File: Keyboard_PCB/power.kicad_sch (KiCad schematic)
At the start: 9 parts, among them U5 ISL91127IRAZ

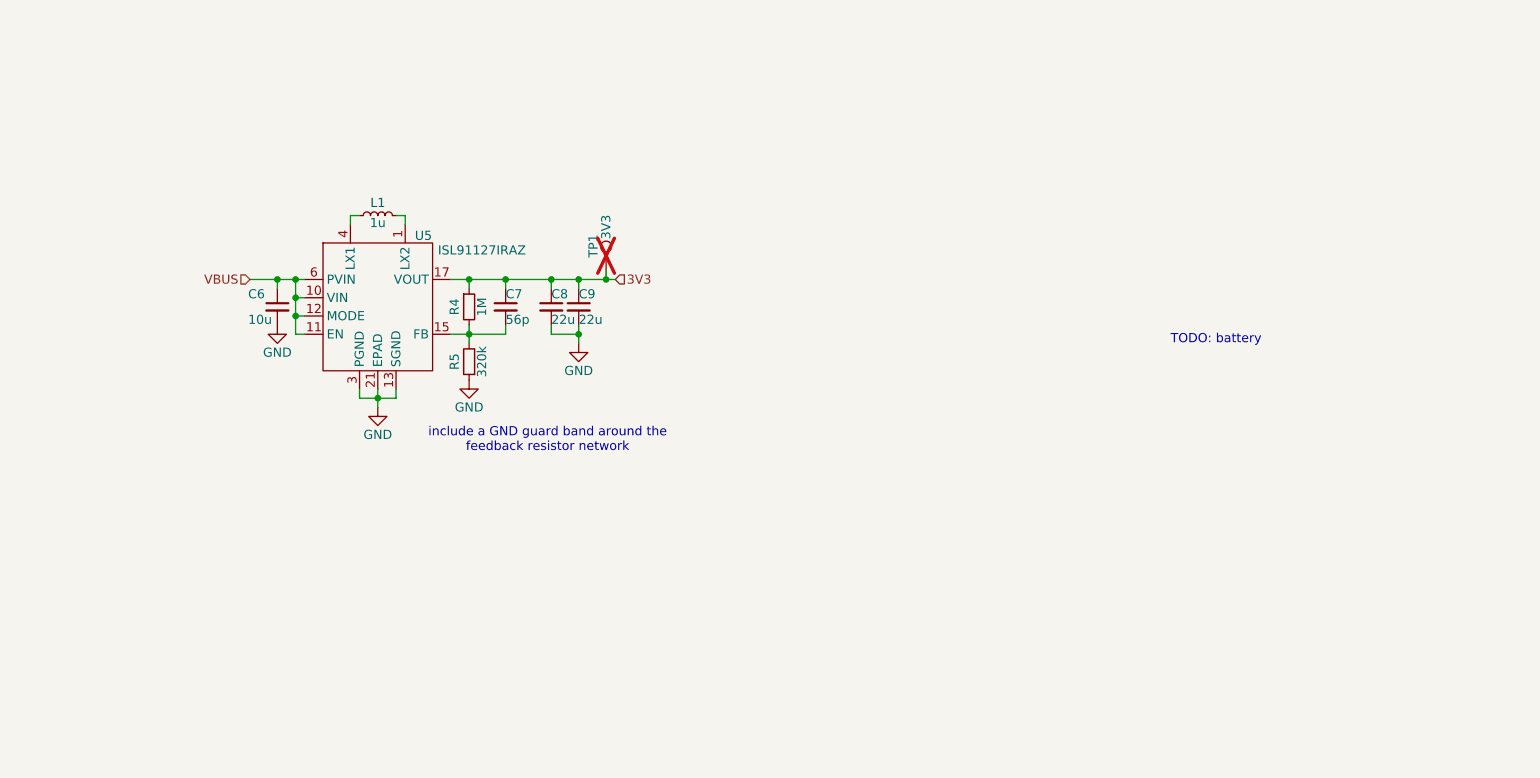
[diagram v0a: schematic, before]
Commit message: Schematic done
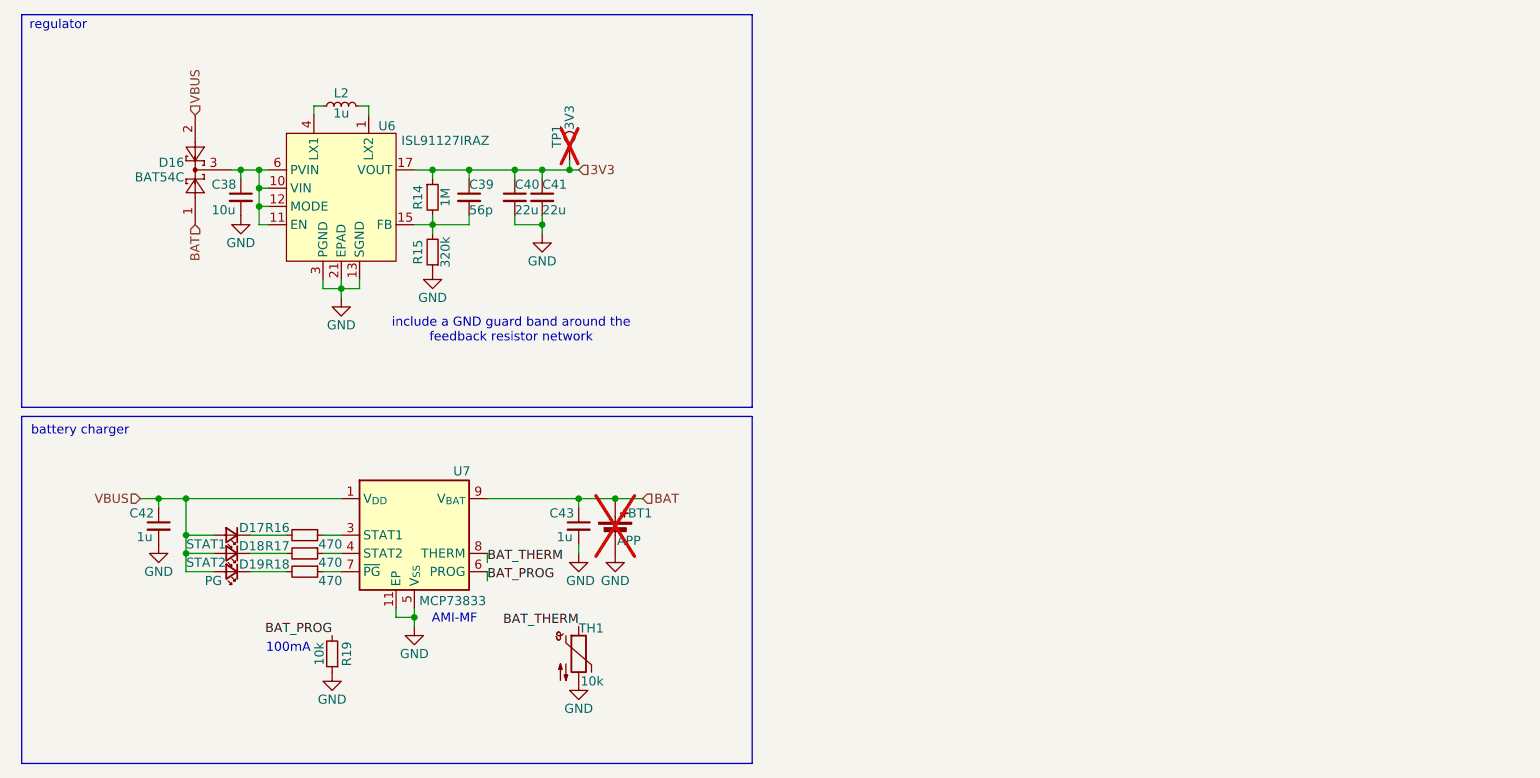
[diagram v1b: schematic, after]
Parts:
- added BT1: APP, Connector_PinHeader_2.54mm:PinHeader_1x02_P2.54mm_Vertical, symbol Device:Battery_Cell
- added C42, C43: 1u, Capacitor_SMD:C_0603_1608Metric, symbol Device:C_Small
- added D16: BAT54C, Package_TO_SOT_SMD:SOT-23, symbol Diode:BAT54C
- added D17: STAT1, LED_SMD:LED_0603_1608Metric, symbol Device:LED_Small
- added D18: STAT2, LED_SMD:LED_0603_1608Metric, symbol Device:LED_Small
- added D19: PG, LED_SMD:LED_0603_1608Metric, symbol Device:LED_Small
- added R16, R17, R18: 470, Resistor_SMD:R_0603_1608Metric, symbol Device:R_Small
- added R19: 10k, Resistor_SMD:R_0603_1608Metric, symbol Device:R_Small
- added TH1: 10k, Resistor_SMD:R_0603_1608Metric, symbol Device:Thermistor_NTC
- added U7: MCP73833, Package_DFN_QFN:DFN-10-1EP_3x3mm_P0.5mm_EP1.58x2.35mm, symbol Battery_Management:MCP73833-xxx-MF
- renumbered C6 to C38, C7 to C39, C8 to C40, C9 to C41, L1 to L2, R4 to R14, R5 to R15, U5 to U6
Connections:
- net GND: now also BT1.2 (-), C42.2, C43.2, R19.1, TH1.2, U7.11 (EP), U7.5 (V_{SS})
- net VBUS: now also C42.1, D16.2, D17.2 (A), D18.2 (A), D19.2 (A), U7.1 (V_{DD}), U7.2 (V_{DD}); no longer C38.1, U6.10 (VIN), U6.11 (EN), U6.12 (MODE), U6.6 (PVIN), U6.7 (PVIN), U6.8 (PVIN), U6.9 (PVIN)
- new net: C38.1, D16.3, U6.10 (VIN), U6.11 (EN), U6.12 (MODE), U6.6 (PVIN), U6.7 (PVIN), U6.8 (PVIN), U6.9 (PVIN)
- new net: R16.1, U7.3 (STAT1)
- new net: R17.1, U7.4 (STAT2)
- new net: R18.1, U7.7 (~{PG})
- new net: D18.1 (K), R17.2
- new net: D17.1 (K), R16.2
- new net: D19.1 (K), R18.2
- new net BAT: BT1.1 (+), C43.1, D16.1, U7.10 (V_{BAT}), U7.9 (V_{BAT})
- new net BAT_PROG: R19.2, U7.6 (PROG)
- new net BAT_THERM: TH1.1, U7.8 (THERM)
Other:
- note added: "100mA"
- note added: "AMI-MF"
- note added: "battery charger"
- note added: "regulator"
- note removed: "TODO: battery"
- moved on the sheet: C38, C39, C40, C41, L2, R14, R15, TP1

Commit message: eMMC routing and STM passives
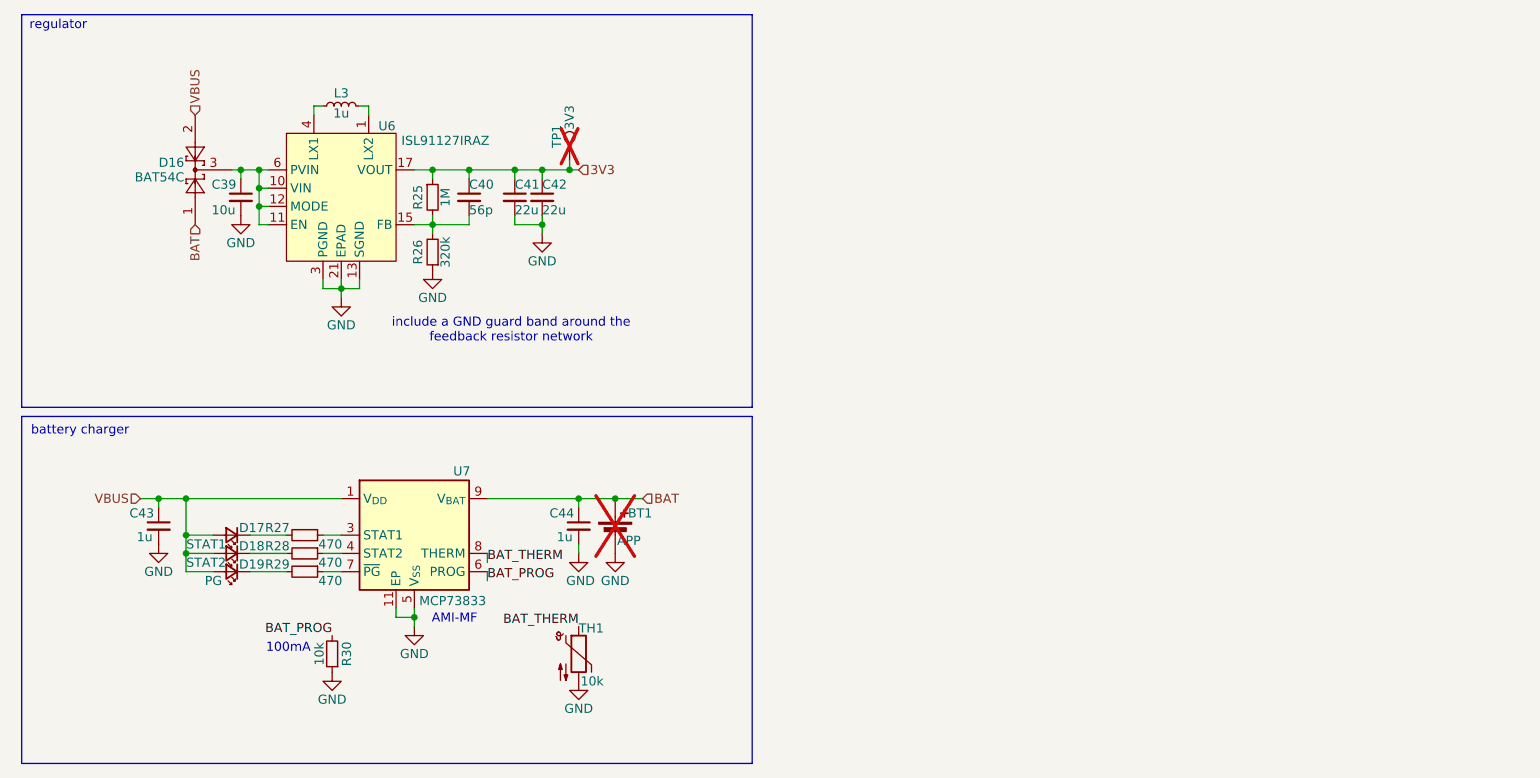
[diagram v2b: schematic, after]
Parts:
- renumbered C38 to C39, C39 to C40, C40 to C41, C41 to C42, C42 to C43, C43 to C44, L2 to L3, R14 to R25, R15 to R26, R16 to R27, R17 to R28, R18 to R29, R19 to R30
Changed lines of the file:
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@@
 		(on_board yes)
 		(dnp no)
-		(property "Reference" "C39"
+		(property "Reference" "C40"
 			(at 74.93 36.322 0)
 			(effects
@@
 			(project "Keyboard_PCB"
 				(path "/dd51e792-c76c-4d43-96de-494177f3b593/700844a0-d855-4a8d-a339-68e2adaa6562"
-					(reference "C39")
+					(reference "C40")
 					(unit 1)
 				)
@@
 		(on_board yes)
 		(dnp no)
-		(property "Reference" "#PWR068"
+		(property "Reference" "#PWR081"
 			(at 67.31 104.14 0)
 			(effects
@@
 			(project "Keyboard_PCB"
 				(path "/dd51e792-c76c-4d43-96de-494177f3b593/700844a0-d855-4a8d-a339-68e2adaa6562"
-					(reference "#PWR068")
+					(reference "#PWR081")
 					(unit 1)
 				)
@@
 		(on_board yes)
 		(dnp no)
-		(property "Reference" "C38"
+		(property "Reference" "C39"
 			(at 39.116 36.322 0)
 			(effects
@@
 			(project "Keyboard_PCB"
 				(path "/dd51e792-c76c-4d43-96de-494177f3b593/700844a0-d855-4a8d-a339-68e2adaa6562"
-					(reference "C38")
+					(reference "C39")
 					(unit 1)
 				)
@@
 		(on_board yes)
 		(dnp no)
-		(property "Reference" "R14"
+		(property "Reference" "R25"
 			(at 67.818 38.1 90)
 			(effects
@@
 			(project "Keyboard_PCB"
 				(path "/dd51e792-c76c-4d43-96de-494177f3b593/700844a0-d855-4a8d-a339-68e2adaa6562"
-					(reference "R14")
+					(reference "R25")
 					(unit 1)
 				)
@@
 		(on_board yes)
 		(dnp no)
-		(property "Reference" "R19"
+		(property "Reference" "R30"
 			(at 57.912 101.6 90)
 			(effects
@@
 			(project "Keyboard_PCB"
 				(path "/dd51e792-c76c-4d43-96de-494177f3b593/700844a0-d855-4a8d-a339-68e2adaa6562"
-					(reference "R19")
+					(reference "R30")
 					(unit 1)
 				)
@@
 		(on_board yes)
 		(dnp no)
-		(property "Reference" "R17"
+		(property "Reference" "R28"
 			(at 48.26 86.614 90)
 			(effects
@@
 			(project "Keyboard_PCB"
 				(path "/dd51e792-c76c-4d43-96de-494177f3b593/700844a0-d855-4a8d-a339-68e2adaa6562"
-					(reference "R17")
+					(reference "R28")
 					(unit 1)
 				)
@@
 		(on_board yes)
 		(dnp no)
-		(property "Reference" "#PWR065"
+		(property "Reference" "#PWR078"
 			(at 31.75 92.71 0)
 			(effects
@@
 			(project "Keyboard_PCB"
 				(path "/dd51e792-c76c-4d43-96de-494177f3b593/700844a0-d855-4a8d-a339-68e2adaa6562"
-					(reference "#PWR065")
+					(reference "#PWR078")
 					(unit 1)
 				)
@@
 		(on_board yes)
 		(dnp no)
-		(property "Reference" "#PWR070"
+		(property "Reference" "#PWR083"
 			(at 90.17 111.76 0)
 			(effects
@@
 			(project "Keyboard_PCB"
 				(path "/dd51e792-c76c-4d43-96de-494177f3b593/700844a0-d855-4a8d-a339-68e2adaa6562"
-					(reference "#PWR070")
+					(reference "#PWR083")
 					(unit 1)
 				)
@@
 		(on_board yes)
 		(dnp no)
-		(property "Reference" "R15"
+		(property "Reference" "R26"
 			(at 67.818 45.72 90)
 			(effects
@@
 			(project "Keyboard_PCB"
 				(path "/dd51e792-c76c-4d43-96de-494177f3b593/700844a0-d855-4a8d-a339-68e2adaa6562"
-					(reference "R15")
+					(reference "R26")
 					(unit 1)
 				)
@@
 		(on_board yes)
 		(dnp no)
-		(property "Reference" "C42"
+		(property "Reference" "C43"
 			(at 27.686 82.042 0)
 			(effects
@@
 			(project "Keyboard_PCB"
 				(path "/dd51e792-c76c-4d43-96de-494177f3b593/700844a0-d855-4a8d-a339-68e2adaa6562"
-					(reference "C42")
+					(reference "C43")
 					(unit 1)
 				)
@@
 		(on_board yes)
 		(dnp no)
-		(property "Reference" "#PWR061"
+		(property "Reference" "#PWR074"
 			(at 43.18 46.99 0)
 			(effects
@@
 			(project "Keyboard_PCB"
 				(path "/dd51e792-c76c-4d43-96de-494177f3b593/700844a0-d855-4a8d-a339-68e2adaa6562"
-					(reference "#PWR061")
+					(reference "#PWR074")
 					(unit 1)
 				)
@@
 		(on_board yes)
 		(dnp no)
-		(property "Reference" "C41"
+		(property "Reference" "C42"
 			(at 85.09 36.322 0)
 			(effects
@@
 			(project "Keyboard_PCB"
 				(path "/dd51e792-c76c-4d43-96de-494177f3b593/700844a0-d855-4a8d-a339-68e2adaa6562"
-					(reference "C41")
+					(reference "C42")
 					(unit 1)
 				)
@@
 		(on_board yes)
 		(dnp no)
-		(property "Reference" "#PWR067"
+		(property "Reference" "#PWR080"
 			(at 95.25 93.98 0)
 			(effects
@@
 			(project "Keyboard_PCB"
 				(path "/dd51e792-c76c-4d43-96de-494177f3b593/700844a0-d855-4a8d-a339-68e2adaa6562"
-					(reference "#PWR067")
+					(reference "#PWR080")
 					(unit 1)
 				)
@@
 		(on_board yes)
 		(dnp no)
-		(property "Reference" "R16"
+		(property "Reference" "R27"
 			(at 48.26 84.074 90)
 			(effects
@@
 			(project "Keyboard_PCB"
 				(path "/dd51e792-c76c-4d43-96de-494177f3b593/700844a0-d855-4a8d-a339-68e2adaa6562"
-					(reference "R16")
+					(reference "R27")
 					(unit 1)
 				)
@@
 		(on_board yes)
 		(dnp no)
-		(property "Reference" "C40"
+		(property "Reference" "C41"
 			(at 81.28 36.322 0)
 			(effects
@@
 			(project "Keyboard_PCB"
 				(path "/dd51e792-c76c-4d43-96de-494177f3b593/700844a0-d855-4a8d-a339-68e2adaa6562"
-					(reference "C40")
+					(reference "C41")
 					(unit 1)
 				)
@@
 		(on_board yes)
 		(dnp no)
-		(property "Reference" "#PWR063"
+		(property "Reference" "#PWR076"
 			(at 69.85 54.61 0)
 			(effects
@@
 			(project "Keyboard_PCB"
 				(path "/dd51e792-c76c-4d43-96de-494177f3b593/700844a0-d855-4a8d-a339-68e2adaa6562"
-					(reference "#PWR063")
+					(reference "#PWR076")
 					(unit 1)
 				)
@@
 		(on_board yes)
 		(dnp no)
-		(property "Reference" "C43"
+		(property "Reference" "C44"
 			(at 86.106 82.042 0)
 			(effects
@@
 			(project "Keyboard_PCB"
 				(path "/dd51e792-c76c-4d43-96de-494177f3b593/700844a0-d855-4a8d-a339-68e2adaa6562"
-					(reference "C43")
+					(reference "C44")
 					(unit 1)
 				)
@@
 		(on_board yes)
 		(dnp no)
-		(property "Reference" "#PWR064"
+		(property "Reference" "#PWR077"
 			(at 57.15 58.42 0)
 			(effects
@@
 			(project "Keyboard_PCB"
 				(path "/dd51e792-c76c-4d43-96de-494177f3b593/700844a0-d855-4a8d-a339-68e2adaa6562"
-					(reference "#PWR064")
+					(reference "#PWR077")
 					(unit 1)
 				)
@@
 		(on_board yes)
 		(dnp no)
-		(property "Reference" "R18"
+		(property "Reference" "R29"
 			(at 48.26 89.154 90)
 			(effects
@@
 			(project "Keyboard_PCB"
 				(path "/dd51e792-c76c-4d43-96de-494177f3b593/700844a0-d855-4a8d-a339-68e2adaa6562"
-					(reference "R18")
+					(reference "R29")
 					(unit 1)
 				)
@@
 		(on_board yes)
 		(dnp no)
-		(property "Reference" "L2"
+		(property "Reference" "L3"
 			(at 57.15 23.622 90)
 			(effects
@@
 			(project "Keyboard_PCB"
 				(path "/dd51e792-c76c-4d43-96de-494177f3b593/700844a0-d855-4a8d-a339-68e2adaa6562"
-					(reference "L2")
+					(reference "L3")
 					(unit 1)
 				)
@@
 		(on_board yes)
 		(dnp no)
-		(property "Reference" "#PWR066"
+		(property "Reference" "#PWR079"
 			(at 90.17 93.98 0)
 			(effects
@@
 			(project "Keyboard_PCB"
 				(path "/dd51e792-c76c-4d43-96de-494177f3b593/700844a0-d855-4a8d-a339-68e2adaa6562"
-					(reference "#PWR066")
+					(reference "#PWR079")
 					(unit 1)
 				)
@@
 		(on_board yes)
 		(dnp no)
-		(property "Reference" "#PWR069"
+		(property "Reference" "#PWR082"
 			(at 55.88 110.49 0)
 			(effects
@@
 			(project "Keyboard_PCB"
 				(path "/dd51e792-c76c-4d43-96de-494177f3b593/700844a0-d855-4a8d-a339-68e2adaa6562"
-					(reference "#PWR069")
+					(reference "#PWR082")
 					(unit 1)
 				)
@@
 		(on_board yes)
 		(dnp no)
-		(property "Reference" "#PWR062"
+		(property "Reference" "#PWR075"
 			(at 85.09 49.53 0)
 			(effects
@@
 			(project "Keyboard_PCB"
 				(path "/dd51e792-c76c-4d43-96de-494177f3b593/700844a0-d855-4a8d-a339-68e2adaa6562"
-					(reference "#PWR062")
-					(unit 1)
-				)
+					(reference "#PWR075")
+					(unit 1)
+				)

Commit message: Layout progress
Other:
- note added: "ISL91127 → Ferrite (e.g., 600Ω @ 100MHz) → 10µF + 100nF → eMMC VCCQ | GND"
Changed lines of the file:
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@@
+		)
+	)
+	(text "ISL91127  →  Ferrite (e.g., 600Ω @ 100MHz) →  10µF + 100nF →  eMMC VCCQ\n                                     |\n                                  GND\n"
+		(exclude_from_sim no)
+		(at 148.59 39.116 0)
+		(effects
+			(font
+				(size 1.27 1.27)
+			)
 		)
 	)

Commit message: Added mouser IDs to components and checked STM-eMMC connection
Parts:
- BT1, D16, L3, R25, R26, R27, R28, R29, R30, TH1, TP1, U6, U7: now left out of the parts list
- C39: mouser 187-CL10A106MQ8NNND -> (none); now left out of the parts list
- C40, C41, C42: mouser 187-CL10A226MP8NUNE -> (none); now left out of the parts list
- C43, C44: mouser 963-MLAST168SB7105KT -> (none); now left out of the parts list
- D17, D18: mouser 710-150060AS75000 -> (none); now left out of the parts list
- D19: mouser 710-150060RS75000 -> (none); now left out of the parts list
